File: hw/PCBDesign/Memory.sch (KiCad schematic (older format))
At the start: 2 parts

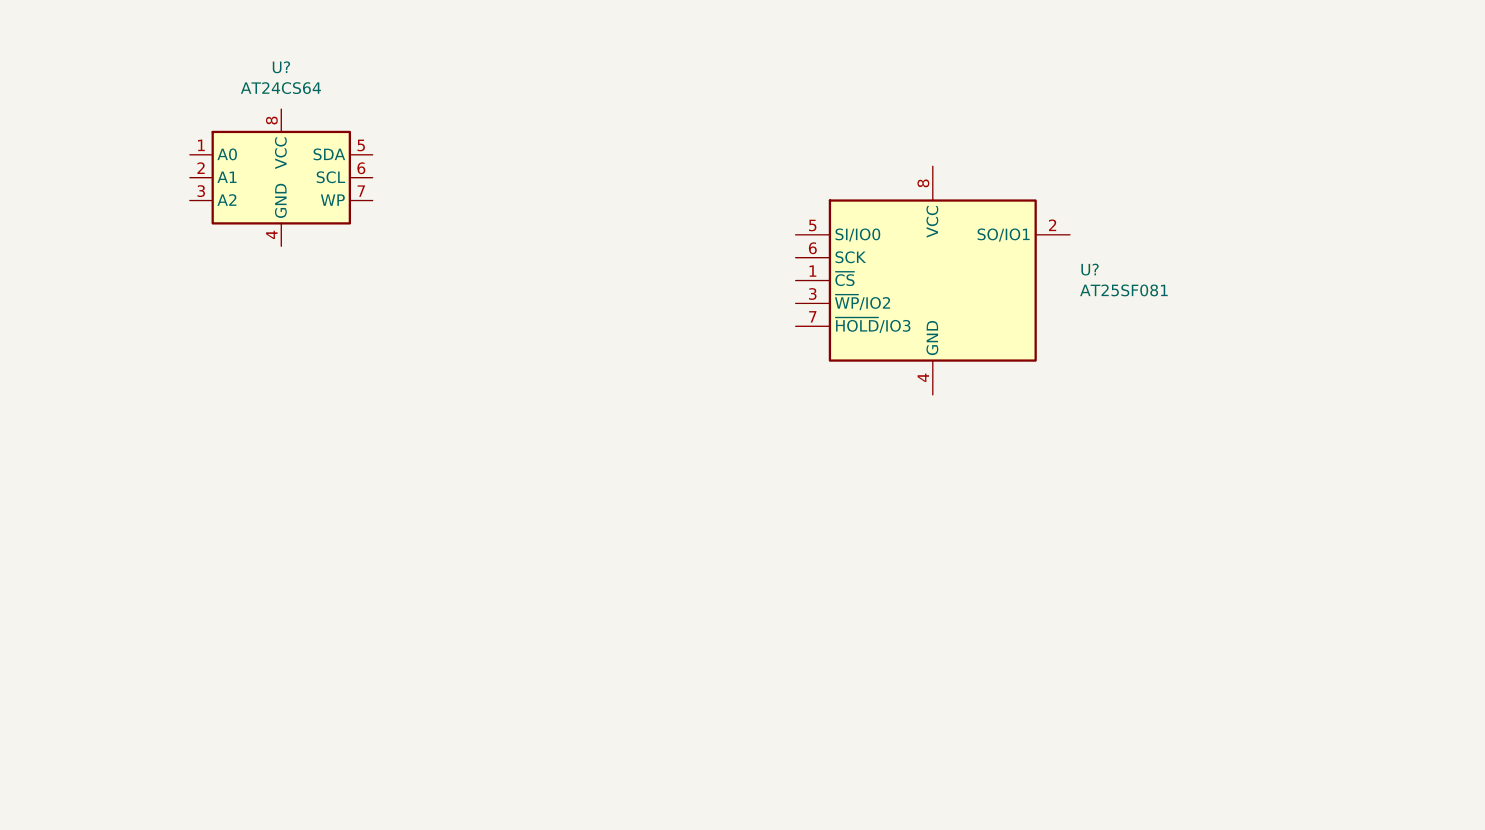
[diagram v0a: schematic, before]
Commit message: Fill out a lot of the board schematic
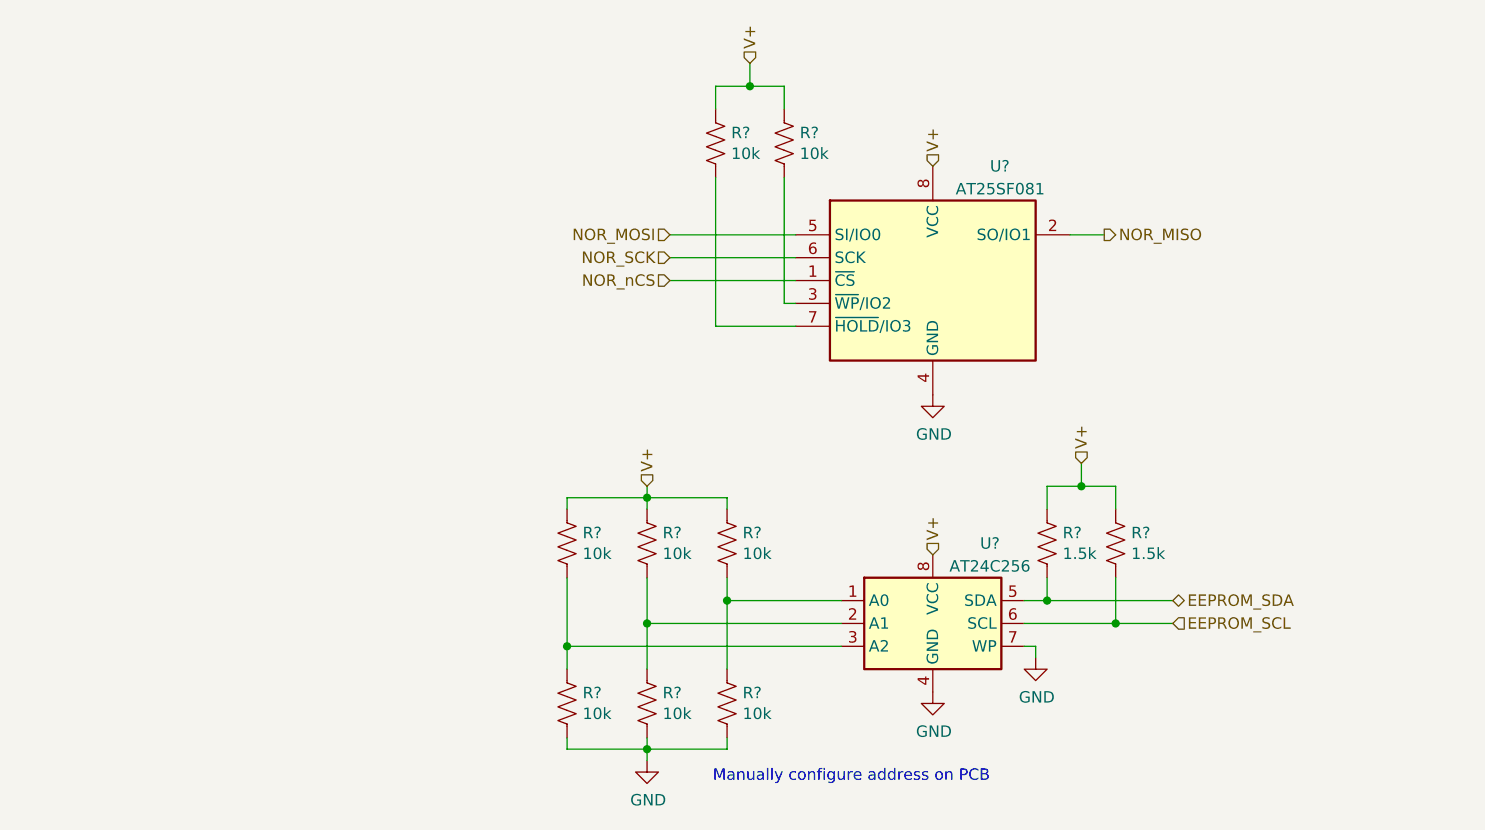
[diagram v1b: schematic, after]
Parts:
- added R? (x8): 10k, symbol Device:R_US
- added R? (x2): 1.5k, symbol Device:R_US
- U?: value AT24CS64 -> AT24C256; LCSC (none) -> C6482
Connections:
- net at U?.1 (A0): now also R?.1, R?.2
- net at U?.2 (A1): now also R?.1, R?.2
- net at U?.3 (A2): now also R?.1, R?.2
- net GND: now reaches U?.4 (GND)
- net GND: now also U?.4 (GND), U?.7 (WP), R?.2, R?.2, R?.2
- net EEPROM_SDA: now reaches U?.5 (SDA)
- net EEPROM_SDA: now also R?.2
- net EEPROM_SCL: now reaches U?.6 (SCL)
- net EEPROM_SCL: now also R?.2
- net V+: now reaches U?.8 (VCC)
- net V+: now also U?.8 (VCC), R?.1, R?.1, R?.1, R?.1, R?.1, R?.1, R?.1
- net NOR_nCS: now reaches U?.1 (~CS)
- net NOR_MISO: now reaches U?.2 (SO/IO1)
- net at U?.3 (~WP~/IO2): now also R?.2
- net NOR_MOSI: now reaches U?.5 (SI/IO0)
- net NOR_SCK: now reaches U?.6 (SCK)
- net at U?.7 (~HOLD~/IO3): now also R?.2
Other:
- note added: "Manually configure address on PCB"
- moved on the sheet: U?

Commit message: Schematic polishing
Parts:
- R60, R61, R62, R63, R64, R65, R66, R67: renamed from R?; footprint (none) -> Resistor_SMD:R_0402_1005Metric; LCSC (none) -> C25744
- R68, R69: renamed from R?; footprint (none) -> Resistor_SMD:R_0402_1005Metric; LCSC (none) -> C25867
- gave numbers to parts that had none: 2
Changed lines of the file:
@@
 $EndDescr
 $Comp
-L Memory_EEPROM:AT24CS64-SSHM U?
+L Memory_EEPROM:AT24CS64-SSHM U5
 U 1 1 6046D99A
 P 5950 4300
-F 0 "U?" H 6200 4650 50  0000 C CNN
+F 0 "U5" H 6200 4650 50  0000 C CNN
 F 1 "AT24C256" H 6200 4550 50  0000 C CNN
 F 2 "Package_SO:SOIC-8_3.9x4.9mm_P1.27mm" H 5950 4300 50  0001 C CNN
@@
 $EndComp
 $Comp
-L Memory_Flash:AT25SF081-SSHD-X U?
+L Memory_Flash:AT25SF081-SSHD-X U4
 U 1 1 6046ED84
 P 5950 2800
-F 0 "U?" H 6200 3300 50  0000 L CNN
+F 0 "U4" H 6200 3300 50  0000 L CNN
 F 1 "AT25SF081" H 6050 3200 50  0000 L CNN
 F 2 "Package_SO:SOIC-8_3.9x4.9mm_P1.27mm" H 5950 2200 50  0001 C CNN
@@
 V+
 $Comp
-L power:GND #PWR?
+L power:GND #PWR073
 U 1 1 60638B7F
 P 5950 3300
-F 0 "#PWR?" H 5950 3050 50  0001 C CNN
+F 0 "#PWR073" H 5950 3050 50  0001 C CNN
 F 1 "GND" H 5955 3127 50  0000 C CNN
 F 2 "" H 5950 3300 50  0001 C CNN
@@
 NOR_nCS
 $Comp
-L Device:R_US R?
+L Device:R_US R62
 U 1 1 60639F64
 P 4700 3950
-F 0 "R?" H 4768 3996 50  0000 L CNN
+F 0 "R62" H 4768 3996 50  0000 L CNN
 F 1 "10k" H 4768 3905 50  0000 L CNN
-F 2 "" V 4740 3940 50  0001 C CNN
+F 2 "Resistor_SMD:R_0402_1005Metric" V 4740 3940 50  0001 C CNN
 F 3 "~" H 4700 3950 50  0001 C CNN
+F 4 "C25744" H 4700 3950 50  0001 C CNN "LCSC"
 	1    4700 3950
 	1    0    0    -1
 $EndComp
 $Comp
-L Device:R_US R?
+L Device:R_US R65
 U 1 1 6063A22F
 P 5050 3950
-F 0 "R?" H 5118 3996 50  0000 L CNN
+F 0 "R65" H 5118 3996 50  0000 L CNN
 F 1 "10k" H 5118 3905 50  0000 L CNN
-F 2 "" V 5090 3940 50  0001 C CNN
+F 2 "Resistor_SMD:R_0402_1005Metric" V 5090 3940 50  0001 C CNN
 F 3 "~" H 5050 3950 50  0001 C CNN
+F 4 "C25744" H 5050 3950 50  0001 C CNN "LCSC"
 	1    5050 3950
 	1    0    0    -1
 $EndComp
 $Comp
-L Device:R_US R?
+L Device:R_US R60
 U 1 1 6063A4AF
 P 4350 3950
-F 0 "R?" H 4418 3996 50  0000 L CNN
+F 0 "R60" H 4418 3996 50  0000 L CNN
 F 1 "10k" H 4418 3905 50  0000 L CNN
-F 2 "" V 4390 3940 50  0001 C CNN
+F 2 "Resistor_SMD:R_0402_1005Metric" V 4390 3940 50  0001 C CNN
 F 3 "~" H 4350 3950 50  0001 C CNN
+F 4 "C25744" H 4350 3950 50  0001 C CNN "LCSC"
 	1    4350 3950
 	1    0    0    -1
 $EndComp
 $Comp
-L Device:R_US R?
+L Device:R_US R66
 U 1 1 6063AB62
 P 5050 4650
-F 0 "R?" H 5118 4696 50  0000 L CNN
+F 0 "R66" H 5118 4696 50  0000 L CNN
 F 1 "10k" H 5118 4605 50  0000 L CNN
-F 2 "" V 5090 4640 50  0001 C CNN
+F 2 "Resistor_SMD:R_0402_1005Metric" V 5090 4640 50  0001 C CNN
 F 3 "~" H 5050 4650 50  0001 C CNN
+F 4 "C25744" H 5050 4650 50  0001 C CNN "LCSC"
 	1    5050 4650
 	1    0    0    -1
 $EndComp
 $Comp
-L Device:R_US R?
+L Device:R_US R63
 U 1 1 6063B6D5
 P 4700 4650
-F 0 "R?" H 4768 4696 50  0000 L CNN
+F 0 "R63" H 4768 4696 50  0000 L CNN
 F 1 "10k" H 4768 4605 50  0000 L CNN
-F 2 "" V 4740 4640 50  0001 C CNN
+F 2 "Resistor_SMD:R_0402_1005Metric" V 4740 4640 50  0001 C CNN
 F 3 "~" H 4700 4650 50  0001 C CNN
+F 4 "C25744" H 4700 4650 50  0001 C CNN "LCSC"
 	1    4700 4650
 	1    0    0    -1
 $EndComp
 $Comp
-L Device:R_US R?
+L Device:R_US R61
 U 1 1 6063BCD1
 P 4350 4650
-F 0 "R?" H 4418 4696 50  0000 L CNN
+F 0 "R61" H 4418 4696 50  0000 L CNN
 F 1 "10k" H 4418 4605 50  0000 L CNN
-F 2 "" V 4390 4640 50  0001 C CNN
+F 2 "Resistor_SMD:R_0402_1005Metric" V 4390 4640 50  0001 C CNN
 F 3 "~" H 4350 4650 50  0001 C CNN
+F 4 "C25744" H 4350 4650 50  0001 C CNN "LCSC"
 	1    4350 4650
 	1    0    0    -1
@@
 Connection ~ 5050 4200
 $Comp
-L power:GND #PWR?
+L power:GND #PWR072
 U 1 1 6063CB47
 P 4700 4900
-F 0 "#PWR?" H 4700 4650 50  0001 C CNN
+F 0 "#PWR072" H 4700 4650 50  0001 C CNN
 F 1 "GND" H 4705 4727 50  0000 C CNN
 F 2 "" H 4700 4900 50  0001 C CNN
@@
 $EndComp
 $Comp
-L power:GND #PWR?
+L power:GND #PWR074
 U 1 1 6063CF26
 P 5950 4600
-F 0 "#PWR?" H 5950 4350 50  0001 C CNN
+F 0 "#PWR074" H 5950 4350 50  0001 C CNN
 F 1 "GND" H 5955 4427 50  0000 C CNN
 F 2 "" H 5950 4600 50  0001 C CNN
@@
 Manually configure address on PCB
 $Comp
-L power:GND #PWR?
+L power:GND #PWR075
 U 1 1 6063E8A1
 P 6400 4450
-F 0 "#PWR?" H 6400 4200 50  0001 C CNN
+F 0 "#PWR075" H 6400 4200 50  0001 C CNN
 F 1 "GND" H 6405 4277 50  0000 C CNN
 F 2 "" H 6400 4450 50  0001 C CNN
@@
 	6400 4400 6400 4450
 $Comp
-L Device:R_US R?
+L Device:R_US R68
 U 1 1 6063F01A
 P 6450 3950
-F 0 "R?" H 6518 3996 50  0000 L CNN
+F 0 "R68" H 6518 3996 50  0000 L CNN
 F 1 "1.5k" H 6518 3905 50  0000 L CNN
-F 2 "" V 6490 3940 50  0001 C CNN
+F 2 "Resistor_SMD:R_0402_1005Metric" V 6490 3940 50  0001 C CNN
 F 3 "~" H 6450 3950 50  0001 C CNN
+F 4 "C25867" H 6450 3950 50  0001 C CNN "LCSC"
 	1    6450 3950
 	1    0    0    -1
 $EndComp
 $Comp
-L Device:R_US R?
+L Device:R_US R69
 U 1 1 6063F7EE
 P 6750 3950
-F 0 "R?" H 6818 3996 50  0000 L CNN
+F 0 "R69" H 6818 3996 50  0000 L CNN
 F 1 "1.5k" H 6818 3905 50  0000 L CNN
-F 2 "" V 6790 3940 50  0001 C CNN
+F 2 "Resistor_SMD:R_0402_1005Metric" V 6790 3940 50  0001 C CNN
 F 3 "~" H 6750 3950 50  0001 C CNN
+F 4 "C25867" H 6750 3950 50  0001 C CNN "LCSC"
 	1    6750 3950
 	1    0    0    -1
@@
 Connection ~ 6450 4200
 $Comp
-L Device:R_US R?
+L Device:R_US R67
 U 1 1 6064232C
 P 5300 2200
-F 0 "R?" H 5368 2246 50  0000 L CNN
+F 0 "R67" H 5368 2246 50  0000 L CNN
 F 1 "10k" H 5368 2155 50  0000 L CNN
-F 2 "" V 5340 2190 50  0001 C CNN
+F 2 "Resistor_SMD:R_0402_1005Metric" V 5340 2190 50  0001 C CNN
 F 3 "~" H 5300 2200 50  0001 C CNN
+F 4 "C25744" H 5300 2200 50  0001 C CNN "LCSC"
 	1    5300 2200
 	1    0    0    -1
 $EndComp
 $Comp
-L Device:R_US R?
+L Device:R_US R64
 U 1 1 60642966
 P 5000 2200
-F 0 "R?" H 5068 2246 50  0000 L CNN
+F 0 "R64" H 5068 2246 50  0000 L CNN
 F 1 "10k" H 5068 2155 50  0000 L CNN
-F 2 "" V 5040 2190 50  0001 C CNN
+F 2 "Resistor_SMD:R_0402_1005Metric" V 5040 2190 50  0001 C CNN
 F 3 "~" H 5000 2200 50  0001 C CNN
+F 4 "C25744" H 5000 2200 50  0001 C CNN "LCSC"
 	1    5000 2200
 	1    0    0    -1

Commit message: Lay out more PCB
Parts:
- added C26, C27: 100n, Capacitor_SMD:C_0402_1005Metric, symbol Device:C
- added R99: 10k, Resistor_SMD:R_0402_1005Metric, symbol Device:R_US
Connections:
- net GND: now also C26.2, C27.2
- net NOR_nCS: now also R99.2
- net V+: now also C26.1, C27.1, R99.1
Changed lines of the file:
@@
 Wire Wire Line
 	6700 2600 6550 2600
-Text HLabel 4800 2600 0    50   Input ~ 0
+Text HLabel 4650 2600 0    50   Input ~ 0
 NOR_MOSI
-Text HLabel 4800 2700 0    50   Input ~ 0
+Text HLabel 4650 2700 0    50   Input ~ 0
 NOR_SCK
-Text HLabel 4800 2800 0    50   Input ~ 0
+Text HLabel 4650 2800 0    50   Input ~ 0
 NOR_nCS
 $Comp
@@
 	5300 2900 5300 2350
 Wire Wire Line
-	4800 2600 5350 2600
-Wire Wire Line
-	4800 2700 5350 2700
-Wire Wire Line
-	4800 2800 5350 2800
+	4650 2800 4700 2800
 Text HLabel 5150 1850 1    50   Input ~ 0
 V+
@@
 	5300 1950 5300 2050
 Connection ~ 5150 1950
+$Comp
+L Device:C C?
+U 1 1 60544AA2
+P 7550 2450
+AR Path="/604707FB/60544AA2" Ref="C?"  Part="1"
+AR Path="/60463DC2/60544AA2" Ref="C26"  Part="1"
+F 0 "C26" H 7665 2496 50  0000 L CNN
+F 1 "100n" H 7665 2405 50  0000 L CNN
+F 2 "Capacitor_SMD:C_0402_1005Metric" H 7588 2300 50  0001 C CNN
+F 3 "~" H 7550 2450 50  0001 C CNN
+F 4 "C1525" H 7550 2450 50  0001 C CNN "LCSC"
+	1    7550 2450
+	1    0    0    -1
+$EndComp
+$Comp
+L Device:C C?
+U 1 1 60545508
+P 7950 4150
+AR Path="/604707FB/60545508" Ref="C?"  Part="1"
+AR Path="/60463DC2/60545508" Ref="C27"  Part="1"
+F 0 "C27" H 8065 4196 50  0000 L CNN
+F 1 "100n" H 8065 4105 50  0000 L CNN
+F 2 "Capacitor_SMD:C_0402_1005Metric" H 7988 4000 50  0001 C CNN
+F 3 "~" H 7950 4150 50  0001 C CNN
+F 4 "C1525" H 7950 4150 50  0001 C CNN "LCSC"
+	1    7950 4150
+	1    0    0    -1
+$EndComp
+Text HLabel 7950 4000 1    50   Input ~ 0
+V+
+Text HLabel 7550 2300 1    50   Input ~ 0
+V+
+$Comp
+L power:GND #PWR068
+U 1 1 60545E1F
+P 7550 2600
+F 0 "#PWR068" H 7550 2350 50  0001 C CNN
+F 1 "GND" H 7555 2427 50  0000 C CNN
+F 2 "" H 7550 2600 50  0001 C CNN
+F 3 "" H 7550 2600 50  0001 C CNN
+	1    7550 2600
+	1    0    0    -1
+$EndComp
+$Comp
+L power:GND #PWR070
+U 1 1 605461BE
+P 7950 4300
+F 0 "#PWR070" H 7950 4050 50  0001 C CNN
+F 1 "GND" H 7955 4127 50  0000 C CNN
+F 2 "" H 7950 4300 50  0001 C CNN
+F 3 "" H 7950 4300 50  0001 C CNN
+	1    7950 4300
+	1    0    0    -1
+$EndComp
+$Comp
+L Device:R_US R99
+U 1 1 6069D3D7
+P 4700 2200
+F 0 "R99" H 4768 2246 50  0000 L CNN
+F 1 "10k" H 4768 2155 50  0000 L CNN
+F 2 "Resistor_SMD:R_0402_1005Metric" V 4740 2190 50  0001 C CNN
+F 3 "~" H 4700 2200 50  0001 C CNN
+F 4 "C25744" H 4700 2200 50  0001 C CNN "LCSC"
+	1    4700 2200
+	1    0    0    -1
+$EndComp
+Wire Wire Line
+	4700 2350 4700 2800
+Connection ~ 4700 2800
+Wire Wire Line
+	4700 2050 4700 1950
+Wire Wire Line
+	4700 1950 5000 1950
+Connection ~ 5000 1950
+Wire Wire Line
+	4650 2600 5350 2600
+Wire Wire Line
+	4650 2700 5350 2700
+Wire Wire Line
+	4700 2800 5350 2800
 $EndSCHEMATC

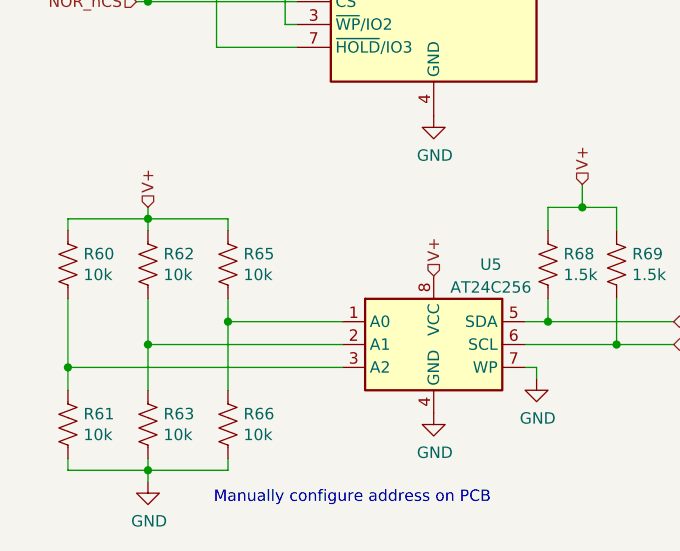
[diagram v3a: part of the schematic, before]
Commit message: Routed most of the core peripherals
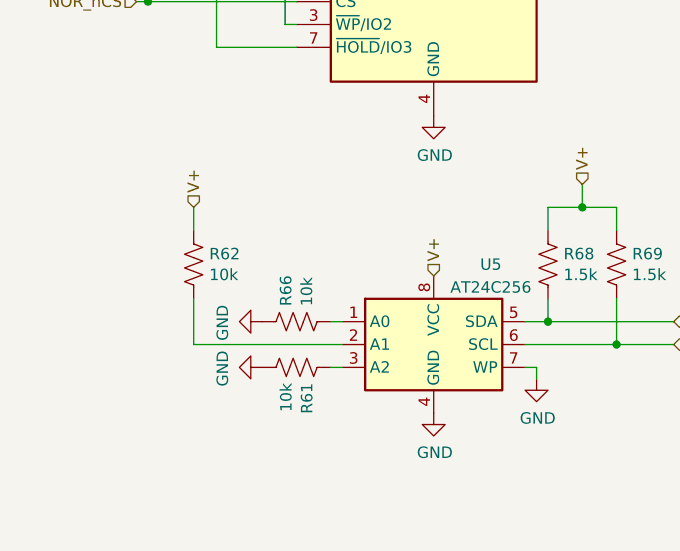
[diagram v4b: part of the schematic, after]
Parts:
- removed R60, R63, R65: 10k, Resistor_SMD:R_0402_1005Metric, symbol Device:R_US
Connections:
- net GND: now also R66.1; no longer R66.2
- net at U5.1 (A0): now also R66.2; no longer R66.1
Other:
- note removed: "Manually configure address on PCB"
- moved on the sheet: R61, R62, R66
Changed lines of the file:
@@
 L Device:R_US R62
 U 1 1 60639F64
-P 4700 3950
-F 0 "R62" H 4768 3996 50  0000 L CNN
-F 1 "10k" H 4768 3905 50  0000 L CNN
-F 2 "Resistor_SMD:R_0402_1005Metric" V 4740 3940 50  0001 C CNN
-F 3 "~" H 4700 3950 50  0001 C CNN
-F 4 "C25744" H 4700 3950 50  0001 C CNN "LCSC"
-	1    4700 3950
-	1    0    0    -1
-$EndComp
-$Comp
-L Device:R_US R65
-U 1 1 6063A22F
-P 5050 3950
-F 0 "R65" H 5118 3996 50  0000 L CNN
-F 1 "10k" H 5118 3905 50  0000 L CNN
-F 2 "Resistor_SMD:R_0402_1005Metric" V 5090 3940 50  0001 C CNN
-F 3 "~" H 5050 3950 50  0001 C CNN
-F 4 "C25744" H 5050 3950 50  0001 C CNN "LCSC"
-	1    5050 3950
-	1    0    0    -1
-$EndComp
-$Comp
-L Device:R_US R60
-U 1 1 6063A4AF
-P 4350 3950
-F 0 "R60" H 4418 3996 50  0000 L CNN
-F 1 "10k" H 4418 3905 50  0000 L CNN
-F 2 "Resistor_SMD:R_0402_1005Metric" V 4390 3940 50  0001 C CNN
-F 3 "~" H 4350 3950 50  0001 C CNN
-F 4 "C25744" H 4350 3950 50  0001 C CNN "LCSC"
-	1    4350 3950
+P 4900 3950
+F 0 "R62" H 4968 3996 50  0000 L CNN
+F 1 "10k" H 4968 3905 50  0000 L CNN
+F 2 "Resistor_SMD:R_0402_1005Metric" V 4940 3940 50  0001 C CNN
+F 3 "~" H 4900 3950 50  0001 C CNN
+F 4 "C25744" H 4900 3950 50  0001 C CNN "LCSC"
+	1    4900 3950
 	1    0    0    -1
 $EndComp
@@
 L Device:R_US R66
 U 1 1 6063AB62
-P 5050 4650
-F 0 "R66" H 5118 4696 50  0000 L CNN
-F 1 "10k" H 5118 4605 50  0000 L CNN
-F 2 "Resistor_SMD:R_0402_1005Metric" V 5090 4640 50  0001 C CNN
-F 3 "~" H 5050 4650 50  0001 C CNN
-F 4 "C25744" H 5050 4650 50  0001 C CNN "LCSC"
-	1    5050 4650
-	1    0    0    -1
-$EndComp
-$Comp
-L Device:R_US R63
-U 1 1 6063B6D5
-P 4700 4650
-F 0 "R63" H 4768 4696 50  0000 L CNN
-F 1 "10k" H 4768 4605 50  0000 L CNN
-F 2 "Resistor_SMD:R_0402_1005Metric" V 4740 4640 50  0001 C CNN
-F 3 "~" H 4700 4650 50  0001 C CNN
-F 4 "C25744" H 4700 4650 50  0001 C CNN "LCSC"
-	1    4700 4650
-	1    0    0    -1
+P 5350 4200
+F 0 "R66" H 5418 4246 50  0000 L CNN
+F 1 "10k" H 5418 4155 50  0000 L CNN
+F 2 "Resistor_SMD:R_0402_1005Metric" V 5390 4190 50  0001 C CNN
+F 3 "~" H 5350 4200 50  0001 C CNN
+F 4 "C25744" H 5350 4200 50  0001 C CNN "LCSC"
+	1    5350 4200
+	0    -1   -1   0
 $EndComp
 $Comp
 L Device:R_US R61
 U 1 1 6063BCD1
-P 4350 4650
-F 0 "R61" H 4418 4696 50  0000 L CNN
-F 1 "10k" H 4418 4605 50  0000 L CNN
-F 2 "Resistor_SMD:R_0402_1005Metric" V 4390 4640 50  0001 C CNN
-F 3 "~" H 4350 4650 50  0001 C CNN
-F 4 "C25744" H 4350 4650 50  0001 C CNN "LCSC"
-	1    4350 4650
-	1    0    0    -1
-$EndComp
-Wire Wire Line
-	5550 4200 5050 4200
-Wire Wire Line
-	5050 4200 5050 4100
-Wire Wire Line
-	5550 4300 4700 4300
-Wire Wire Line
-	4700 4300 4700 4100
-Wire Wire Line
-	5550 4400 4350 4400
-Wire Wire Line
-	4350 4400 4350 4100
-Wire Wire Line
-	4350 4500 4350 4400
-Connection ~ 4350 4400
-Wire Wire Line
-	4700 4500 4700 4300
-Connection ~ 4700 4300
-Wire Wire Line
-	5050 4500 5050 4200
-Connection ~ 5050 4200
+P 5350 4400
+F 0 "R61" H 5418 4446 50  0000 L CNN
+F 1 "10k" H 5418 4355 50  0000 L CNN
+F 2 "Resistor_SMD:R_0402_1005Metric" V 5390 4390 50  0001 C CNN
+F 3 "~" H 5350 4400 50  0001 C CNN
+F 4 "C25744" H 5350 4400 50  0001 C CNN "LCSC"
+	1    5350 4400
+	0    1    1    0
+$EndComp
 $Comp
 L power:GND #PWR072
 U 1 1 6063CB47
-P 4700 4900
-F 0 "#PWR072" H 4700 4650 50  0001 C CNN
-F 1 "GND" H 4705 4727 50  0000 C CNN
-F 2 "" H 4700 4900 50  0001 C CNN
-F 3 "" H 4700 4900 50  0001 C CNN
-	1    4700 4900
-	1    0    0    -1
+P 5200 4400
+F 0 "#PWR072" H 5200 4150 50  0001 C CNN
+F 1 "GND" H 5205 4227 50  0000 C CNN
+F 2 "" H 5200 4400 50  0001 C CNN
+F 3 "" H 5200 4400 50  0001 C CNN
+	1    5200 4400
+	0    1    1    0
 $EndComp
 $Comp
@@
 Text HLabel 5950 4000 1    50   Input ~ 0
 V+
-Text HLabel 4700 3700 1    50   Input ~ 0
-V+
-Wire Wire Line
-	4700 3700 4700 3750
-Wire Wire Line
-	4700 3750 5050 3750
-Wire Wire Line
-	5050 3750 5050 3800
-Connection ~ 4700 3750
-Wire Wire Line
-	4700 3750 4700 3800
-Wire Wire Line
-	4350 3800 4350 3750
-Wire Wire Line
-	4350 3750 4700 3750
-Wire Wire Line
-	4700 4800 4700 4850
-Wire Wire Line
-	4350 4800 4350 4850
-Wire Wire Line
-	4350 4850 4700 4850
-Connection ~ 4700 4850
-Wire Wire Line
-	4700 4850 4700 4900
-Wire Wire Line
-	5050 4850 5050 4800
-Wire Wire Line
-	4700 4850 5050 4850
-Text Notes 6200 5000 2    50   ~ 0
-Manually configure address on PCB
+Text HLabel 4900 3700 1    50   Input ~ 0
+V+
 $Comp
 L power:GND #PWR075
@@
 Wire Wire Line
 	4700 2800 5350 2800
+Wire Wire Line
+	4900 3700 4900 3800
+$Comp
+L power:GND #PWR03
+U 1 1 607575A8
+P 5200 4200
+F 0 "#PWR03" H 5200 3950 50  0001 C CNN
+F 1 "GND" H 5205 4027 50  0000 C CNN
+F 2 "" H 5200 4200 50  0001 C CNN
+F 3 "" H 5200 4200 50  0001 C CNN
+	1    5200 4200
+	0    1    1    0
+$EndComp
+Wire Wire Line
+	5500 4400 5550 4400
+Wire Wire Line
+	5500 4200 5550 4200
+Wire Wire Line
+	4900 4100 4900 4300
+Wire Wire Line
+	4900 4300 5550 4300
 $EndSCHEMATC
